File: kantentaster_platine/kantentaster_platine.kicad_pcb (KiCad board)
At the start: 2 copper layers, 73.7 x 47 mm, 38 parts, among them IC1 PC817, P1 CONN_SENS, P2 CONN_12V, P3 CONN_OUTPUT, P4 lvl high test, P5 sens test, P6 lvl low test, P7 gnd test, Q1 BC817-40, U1 LM317_SOT223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

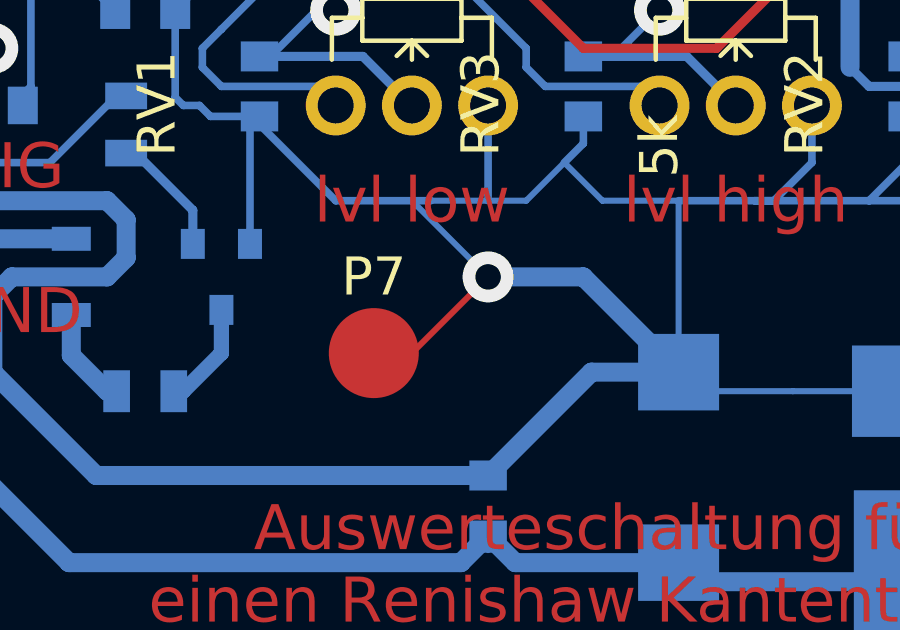
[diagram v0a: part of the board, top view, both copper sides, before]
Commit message: leiterbahn an messpad entfernt (optische Korrektur)
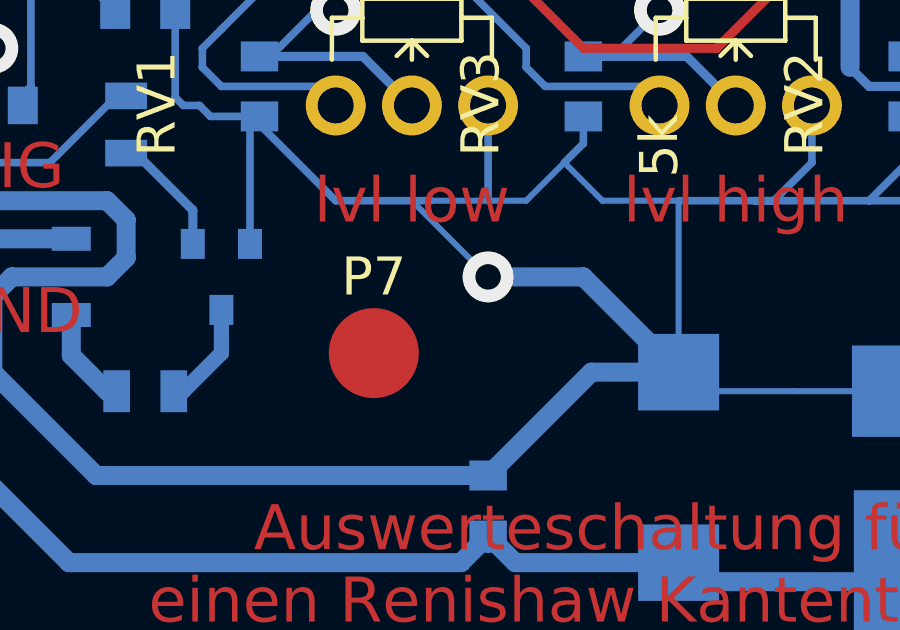
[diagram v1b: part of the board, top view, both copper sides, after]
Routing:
- net GND: track 268.1 -> 264.5 mm
